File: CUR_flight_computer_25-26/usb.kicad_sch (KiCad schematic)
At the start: 0 parts

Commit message: Hook up USB connector
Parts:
- added J1: USB_C_Receptacle_USB2.0_16P, symbol Connector:USB_C_Receptacle_USB2.0_16P
- added R3, R4: 5.1k, symbol Device:R_US
- added U3: USBLC6-2SC6, Package_TO_SOT_SMD:SOT-23-6, symbol Power_Protection:USBLC6-2SC6
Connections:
- new net: J1.B5 (CC2), R4.1
- new net: J1.A5 (CC1), R3.1
- new net: J1.A6 (D+), J1.B6 (D+), U3.3 (I/O2)
- new net: J1.A7 (D-), J1.B7 (D-), U3.1 (I/O1)
- new net +5V: J1.A4 (VBUS), J1.A9 (VBUS), J1.B4 (VBUS), J1.B9 (VBUS), U3.5 (VBUS)
- new net GND: J1.A1 (GND), J1.A12 (GND), J1.B1 (GND), J1.B12 (GND), J1.S1 (SHIELD), R3.2, R4.2, U3.2 (GND)
- new net USB_D+: U3.4 (I/O2)
- new net USB_D-: U3.6 (I/O1)
- no-connect marks 0 -> 2
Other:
- note added: "ESD Protection Place near connector"

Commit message: Use VBUS instead of +5V on usb
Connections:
- net +5V renamed VBUS

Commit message: updated all needed fixes
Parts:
- renumbered J1 to J12, R3 to R46, R4 to R47, U3 to U14
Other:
- moved on the sheet: J12, R46, R47, U14

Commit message: assigned footrpint
need to double check:
- HSE
- Capacitors

for some unknown reason cur kicad library refuses to work
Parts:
- R46, R47: footprint (none) -> Resistor_SMD:R_0603_1608Metric
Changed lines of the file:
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@@
 			)
 		)
-		(property "Footprint" ""
+		(property "Footprint" "Resistor_SMD:R_0603_1608Metric"
 			(at 61.214 45.974 90)
 			(effects
@@
 			)
 		)
-		(property "Footprint" ""
+		(property "Footprint" "Resistor_SMD:R_0603_1608Metric"
 			(at 61.214 43.434 90)
 			(effects

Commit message: assigned usb footprint
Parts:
- J12: footprint (none) -> SAMESKY_UJ20-C-H-G-SMT-P16-TR:SAMESKY_UJ20-C-H-G-SMT-P16-TR
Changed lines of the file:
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@@
 			)
 		)
-		(property "Footprint" ""
+		(property "Footprint" "SAMESKY_UJ20-C-H-G-SMT-P16-TR:SAMESKY_UJ20-C-H-G-SMT-P16-TR"
 			(at 41.91 54.61 0)
 			(effects

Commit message: routing updates
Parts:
- J12: footprint SAMESKY_UJ20-C-H-G-SMT-P16-TR:SAMESKY_UJ20-C-H-G-SMT-P16-TR -> SAMESKY_UJ20-C-H-G-SMT-5-P16-TR:SAMESKY_UJ20-C-H-G-SMT-5-P16-TR
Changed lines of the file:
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@@
 			)
 		)
-		(property "Footprint" "SAMESKY_UJ20-C-H-G-SMT-P16-TR:SAMESKY_UJ20-C-H-G-SMT-P16-TR"
+		(property "Footprint" "SAMESKY_UJ20-C-H-G-SMT-5-P16-TR:SAMESKY_UJ20-C-H-G-SMT-5-P16-TR"
 			(at 41.91 54.61 0)
 			(effects

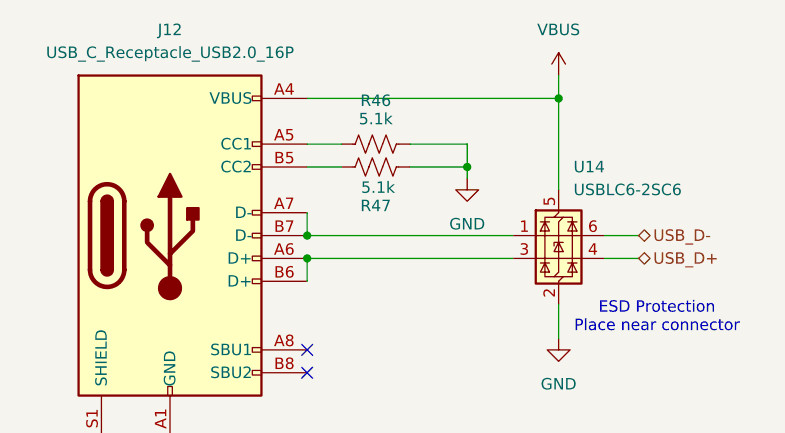
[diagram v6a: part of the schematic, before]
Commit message: Add MPNs for ICs
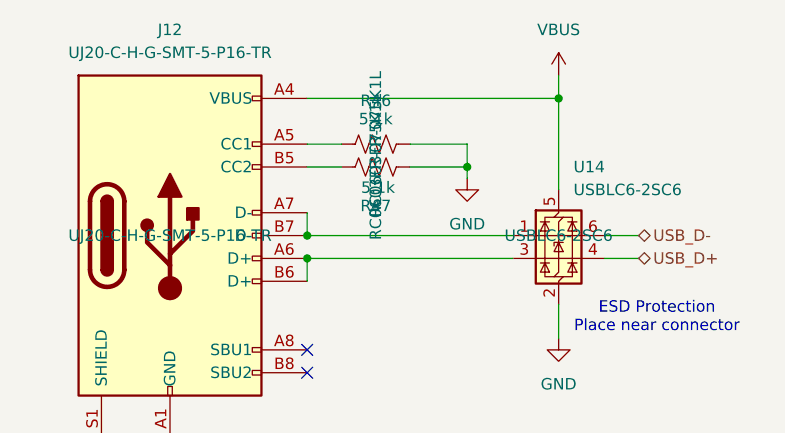
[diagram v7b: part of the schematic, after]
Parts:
- J12: value USB_C_Receptacle_USB2.0_16P -> UJ20-C-H-G-SMT-5-P16-TR; MPN (none) -> UJ20-C-H-G-SMT-5-P16-TR
- R46, R47: MPN (none) -> RC0603FR-075K1L
- U14: MPN (none) -> USBLC6-2SC6
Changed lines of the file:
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@@
+			)
+		)
+		(property "MPN" "RC0603FR-075K1L"
+			(at 60.96 46.99 0)
+			(effects
+				(font
+					(size 1.27 1.27)
+				)
 			)
 		)
@@
 			)
 		)
-		(property "Value" "USB_C_Receptacle_USB2.0_16P"
+		(property "Value" "UJ20-C-H-G-SMT-5-P16-TR"
 			(at 38.1 34.29 0)
 			(effects
@@
 				)
 				(hide yes)
+			)
+		)
+		(property "MPN" "UJ20-C-H-G-SMT-5-P16-TR"
+			(at 38.1 54.61 0)
+			(effects
+				(font
+					(size 1.27 1.27)
+				)
 			)
 		)
@@
 			)
 		)
+		(property "MPN" "USBLC6-2SC6"
+			(at 81.28 54.61 0)
+			(effects
+				(font
+					(size 1.27 1.27)
+				)
+			)
+		)
 		(pin "3"
 		)
@@
 			)
 		)
+		(property "MPN" "RC0603FR-075K1L"
+			(at 60.96 44.45 0)
+			(effects
+				(font
+					(size 1.27 1.27)
+				)
+			)
+		)

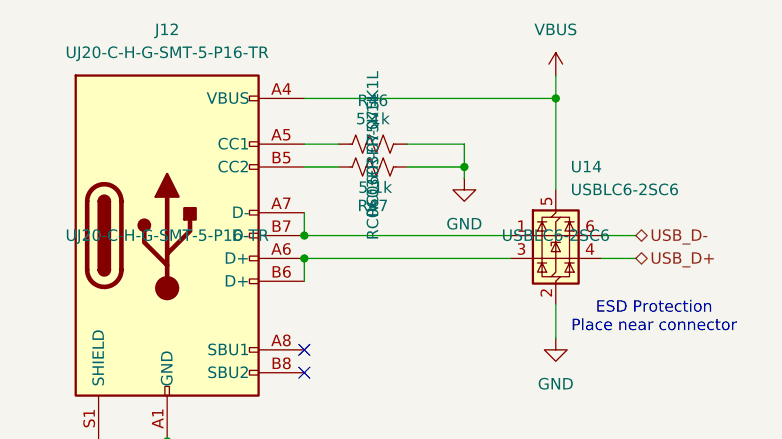
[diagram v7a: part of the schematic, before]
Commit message: Hide MPNs
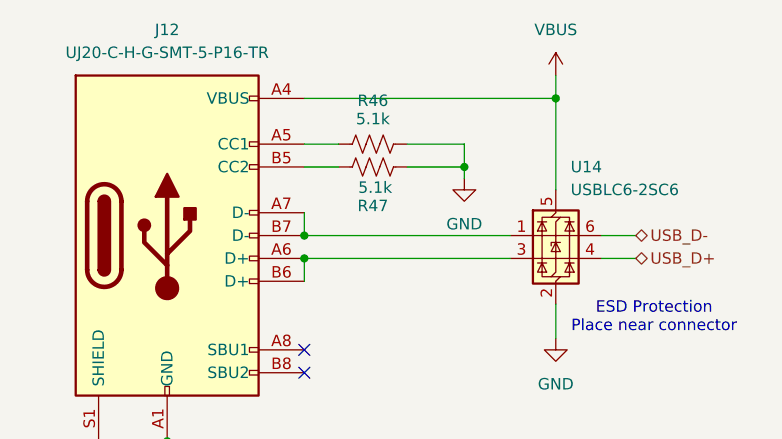
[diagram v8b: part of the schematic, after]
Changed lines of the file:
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@@
 					(size 1.27 1.27)
 				)
+				(hide yes)
 			)
 		)
@@
 					(size 1.27 1.27)
 				)
+				(hide yes)
 			)
 		)
@@
 					(size 1.27 1.27)
 				)
+				(hide yes)
 			)
 		)
@@
 					(size 1.27 1.27)
 				)
-			)
-		)
+				(hide yes)
+			)
+		)
